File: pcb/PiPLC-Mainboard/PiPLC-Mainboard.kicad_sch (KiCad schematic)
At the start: 145 parts, among them J1 WJ2EDGRC-5.08-4P, J10 WJ2EDGRC-5.08-4P, J11 WJ2EDGRC-5.08-4P, J12 WJ2EDGRC-5.08-4P, J13 Modbus, J17 Conn_02x12_Odd_Even, J3 WJ2EDGRC-5.08-4P, J4 WJ2EDGRC-5.08-4P, J5 WJ2EDGRC-5.08-4P, J6 WJ2EDGRC-5.08-4P, J7 WJ2EDGRC-5.08-4P, J8 WJ2EDGRC-5.08-4P, J9 WJ2EDGRC-5.08-4P, J99 Rpi GPIO, K1 G5RL-1A-E-TV8 DC24, K2 G5RL-1A-E-TV8 DC24, K3 G5RL-1A-E-TV8 DC24, K4 G5RL-1A-E-TV8 DC24, K5 G5RL-1A-E-TV8 DC24, K6 G5RL-1A-E-TV8 DC24, K7 G5RL-1A-E-TV8 DC24, K8 G5RL-1A-E-TV8 DC24, Q1 AO3400A, Q2 AO3400A, Q3 AO3400A, Q4 AO3400A, Q5 AO3400A, Q6 AO3400A, Q7 AO3400A, Q8 AO3400A, U1 TPS54331D, U10 EL817C, U11 EL817C, U12 ISO3082DWR, U2 NCN5121, U3 ISO1540, U4 EL817C, U5 EL817C, U6 EL817C, U7 EL817C, U8 EL817C, U9 EL817C, Y2 16MHz

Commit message: [Main] Start positioning parts
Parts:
- renumbered J3 to J1, J8 to J10, J6 to J11, J7 to J12, J13 to J2, J9 to J3, J10 to J4, J11 to J5, J12 to J6, J1 to J7, J4 to J8, J5 to J9
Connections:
- net +3V3: now also J17.7 (Pin_7); no longer J17.8 (Pin_8)
- net GND: now also J17.4 (Pin_4), J17.6 (Pin_6); no longer J17.3 (Pin_3), J17.5 (Pin_5)
- net KNX +: now also J17.8 (Pin_8); no longer J17.7 (Pin_7)
- net LED_I1: now also J17.9 (Pin_9); no longer J17.10 (Pin_10)
- net LED_I2: now also J17.11 (Pin_11); no longer J17.12 (Pin_12)
- net LED_I3: now also J17.13 (Pin_13); no longer J17.14 (Pin_14)
- net LED_I4: now also J17.15 (Pin_15); no longer J17.16 (Pin_16)
- net LED_I5: now also J17.17 (Pin_17); no longer J17.18 (Pin_18)
- net LED_I6: now also J17.19 (Pin_19); no longer J17.20 (Pin_20)
- net LED_I7: now also J17.21 (Pin_21); no longer J17.22 (Pin_22)
- net LED_I8: now also J17.23 (Pin_23); no longer J17.24 (Pin_24)
- net LED_Q1: now also J17.24 (Pin_24); no longer J17.23 (Pin_23)
- net LED_Q2: now also J17.22 (Pin_22); no longer J17.21 (Pin_21)
- net LED_Q3: now also J17.20 (Pin_20); no longer J17.19 (Pin_19)
- net LED_Q4: now also J17.18 (Pin_18); no longer J17.17 (Pin_17)
- net LED_Q5: now also J17.16 (Pin_16); no longer J17.15 (Pin_15)
- net LED_Q6: now also J17.14 (Pin_14); no longer J17.13 (Pin_13)
- net LED_Q7: now also J17.12 (Pin_12); no longer J17.11 (Pin_11)
- net LED_Q8: now also J17.10 (Pin_10); no longer J17.9 (Pin_9)
- net at R8.1: now also J12.4 (Pin_4); no longer J12.1 (Pin_1)
- net at R9.1: now also J12.3 (Pin_3); no longer J12.2 (Pin_2)
- net at R49.2: now also J17.3 (Pin_3); no longer J17.4 (Pin_4)
- net at R45.2: now also J17.5 (Pin_5); no longer J17.6 (Pin_6)
- net at R10.1: now also J12.2 (Pin_2); no longer J12.3 (Pin_3)
- net at R11.1: now also J12.1 (Pin_1); no longer J12.4 (Pin_4)
- net at R13.1: now also J11.3 (Pin_3); no longer J11.2 (Pin_2)
- net at R15.1: now also J11.1 (Pin_1); no longer J11.4 (Pin_4)
- net at R12.1: now also J11.4 (Pin_4); no longer J11.1 (Pin_1)
- net at R14.1: now also J11.2 (Pin_2); no longer J11.3 (Pin_3)
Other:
- moved on the sheet: J11, J12
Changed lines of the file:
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@@
   (symbol (lib_id "Connector_Generic:Conn_01x04") (at 27.94 157.48 0) (mirror y) (unit 1)
     (in_bom yes) (on_board yes) (dnp no)
-    (property "Reference" "J4" (at 27.94 149.86 0)
+    (property "Reference" "J8" (at 27.94 149.86 0)
       (effects (font (size 1.27 1.27)))
     )
@@
       (project "PiPLC-Mainboard"
         (path "/93ebf745-625a-4d9e-8f47-45e91f30ef94"
-          (reference "J4") (unit 1)
+          (reference "J8") (unit 1)
         )
       )
@@
   (symbol (lib_id "Connector_Generic:Conn_01x04") (at 381 353.06 270) (unit 1)
     (in_bom yes) (on_board yes) (dnp no)
-    (property "Reference" "J10" (at 379.73 364.49 90)
+    (property "Reference" "J4" (at 379.73 364.49 90)
       (effects (font (size 1.27 1.27)))
     )
@@
       (project "PiPLC-Mainboard"
         (path "/93ebf745-625a-4d9e-8f47-45e91f30ef94"
-          (reference "J10") (unit 1)
+          (reference "J4") (unit 1)
         )
       )
@@
   (symbol (lib_id "Connector_Generic:Conn_01x04") (at 259.08 353.06 270) (unit 1)
     (in_bom yes) (on_board yes) (dnp no)
-    (property "Reference" "J11" (at 257.81 364.49 90)
+    (property "Reference" "J5" (at 257.81 364.49 90)
       (effects (font (size 1.27 1.27)))
     )
@@
       (project "PiPLC-Mainboard"
         (path "/93ebf745-625a-4d9e-8f47-45e91f30ef94"
-          (reference "J11") (unit 1)
+          (reference "J5") (unit 1)
         )
       )
@@
   (symbol (lib_id "Connector_Generic:Conn_01x04") (at 27.94 189.23 0) (mirror y) (unit 1)
     (in_bom yes) (on_board yes) (dnp no)
-    (property "Reference" "J5" (at 27.94 181.61 0)
+    (property "Reference" "J9" (at 27.94 181.61 0)
       (effects (font (size 1.27 1.27)))
     )
@@
       (project "PiPLC-Mainboard"
         (path "/93ebf745-625a-4d9e-8f47-45e91f30ef94"
-          (reference "J5") (unit 1)
+          (reference "J9") (unit 1)
         )
       )
@@
   (symbol (lib_id "Connector_Generic:Conn_01x04") (at 502.92 353.06 270) (unit 1)
     (in_bom yes) (on_board yes) (dnp no)
-    (property "Reference" "J9" (at 501.65 364.49 90)
+    (property "Reference" "J3" (at 501.65 364.49 90)
       (effects (font (size 1.27 1.27)))
     )
@@
       (project "PiPLC-Mainboard"
         (path "/93ebf745-625a-4d9e-8f47-45e91f30ef94"
-          (reference "J9") (unit 1)
+          (reference "J3") (unit 1)
         )
       )
@@
   (symbol (lib_id "Connector_Generic:Conn_01x04") (at 410.21 160.02 0) (unit 1)
     (in_bom yes) (on_board yes) (dnp no)
-    (property "Reference" "J1" (at 410.21 152.4 0)
+    (property "Reference" "J7" (at 410.21 152.4 0)
       (effects (font (size 1.27 1.27)))
     )
@@
       (project "PiPLC-Mainboard"
         (path "/93ebf745-625a-4d9e-8f47-45e91f30ef94"
-          (reference "J1") (unit 1)
+          (reference "J7") (unit 1)
         )
       )
@@
     )
   )
-  (symbol (lib_id "Connector_Generic:Conn_02x12_Odd_Even") (at 193.04 241.3 90) (unit 1)
-    (in_bom yes) (on_board yes) (dnp no) (fields_autoplaced)
-    (property "Reference" "J17" (at 177.8 238.76 90)
+  (symbol (lib_id "Connector_Generic:Conn_02x12_Odd_Even") (at 193.04 238.76 90) (mirror x) (unit 1)
+    (in_bom yes) (on_board yes) (dnp no)
+    (property "Reference" "J17" (at 177.8 241.3 90)
       (effects (font (size 1.27 1.27)) (justify left))
     )
-    (property "Value" "Conn_02x12_Odd_Even" (at 177.8 241.3 90)
+    (property "Value" "Conn_02x12_Odd_Even" (at 177.8 238.76 90)
       (effects (font (size 1.27 1.27)) (justify left))
     )
-    (property "Footprint" "Connector_PinSocket_2.54mm:PinSocket_2x12_P2.54mm_Vertical" (at 193.04 241.3 0)
+    (property "Footprint" "Connector_PinSocket_2.54mm:PinSocket_2x12_P2.54mm_Vertical" (at 193.04 238.76 0)
       (effects (font (size 1.27 1.27)) hide)
     )
-    (property "Datasheet" "~" (at 193.04 241.3 0)
+    (property "Datasheet" "~" (at 193.04 238.76 0)
       (effects (font (size 1.27 1.27)) hide)
     )
@@
     )
   )
-  (symbol (lib_id "Connector_Generic:Conn_01x04") (at 27.94 30.48 0) (mirror y) (unit 1)
+  (symbol (lib_id "Connector_Generic:Conn_01x04") (at 27.94 33.02 180) (unit 1)
     (in_bom yes) (on_board yes) (dnp no)
-    (property "Reference" "J7" (at 27.94 22.86 0)
+    (property "Reference" "J12" (at 27.94 22.86 0)
       (effects (font (size 1.27 1.27)))
     )
@@
       (effects (font (size 1.27 1.27)))
     )
-    (property "Footprint" "Connector_Phoenix_MSTB:PhoenixContact_MSTBA_2,5_4-G-5,08_1x04_P5.08mm_Horizontal" (at 27.94 30.48 0)
+    (property "Footprint" "Connector_Phoenix_MSTB:PhoenixContact_MSTBA_2,5_4-G-5,08_1x04_P5.08mm_Horizontal" (at 27.94 33.02 0)
       (effects (font (size 1.27 1.27)) hide)
     )
-    (property "Datasheet" "https://datasheet.lcsc.com/lcsc/1912251635_Ningbo-Kangnex-Elec-WJ2EDGRC-5-08-4P_C8446.pdf" (at 27.94 30.48 0)
+    (property "Datasheet" "https://datasheet.lcsc.com/lcsc/1912251635_Ningbo-Kangnex-Elec-WJ2EDGRC-5-08-4P_C8446.pdf" (at 27.94 33.02 0)
       (effects (font (size 1.27 1.27)) hide)
     )
-    (property "LCSC" "C8446" (at 27.94 30.48 0)
+    (property "LCSC" "C8446" (at 27.94 33.02 0)
       (effects (font (size 1.27 1.27)) hide)
     )
@@
       (project "PiPLC-Mainboard"
         (path "/93ebf745-625a-4d9e-8f47-45e91f30ef94"
-          (reference "J7") (unit 1)
+          (reference "J12") (unit 1)
         )
       )
@@
   (symbol (lib_id "Connector_Generic:Conn_01x04") (at 236.22 31.75 0) (mirror y) (unit 1)
     (in_bom yes) (on_board yes) (dnp no)
-    (property "Reference" "J8" (at 231.14 24.13 0)
+    (property "Reference" "J10" (at 231.14 24.13 0)
       (effects (font (size 1.27 1.27)))
     )
@@
       (project "PiPLC-Mainboard"
         (path "/93ebf745-625a-4d9e-8f47-45e91f30ef94"
-          (reference "J8") (unit 1)
+          (reference "J10") (unit 1)
         )
       )
@@
   (symbol (lib_id "Connector_Generic:Conn_01x04") (at 27.94 220.98 0) (mirror y) (unit 1)
     (in_bom yes) (on_board yes) (dnp no)
-    (property "Reference" "J3" (at 27.94 213.36 0)
+    (property "Reference" "J1" (at 27.94 213.36 0)
       (effects (font (size 1.27 1.27)))
     )
@@
       (project "PiPLC-Mainboard"
         (path "/93ebf745-625a-4d9e-8f47-45e91f30ef94"
-          (reference "J3") (unit 1)
+          (reference "J1") (unit 1)
         )
       )
@@
   (symbol (lib_id "Connector_Generic:Conn_01x04") (at 137.16 353.06 270) (unit 1)
     (in_bom yes) (on_board yes) (dnp no)
-    (property "Reference" "J12" (at 135.89 364.49 90)
+    (property "Reference" "J6" (at 135.89 364.49 90)
       (effects (font (size 1.27 1.27)))
     )
@@
       (project "PiPLC-Mainboard"
         (path "/93ebf745-625a-4d9e-8f47-45e91f30ef94"
-          (reference "J12") (unit 1)
+          (reference "J6") (unit 1)
         )
       )
@@
   (symbol (lib_id "Connector_Generic:Conn_01x04") (at 411.48 195.58 0) (unit 1)
     (in_bom yes) (on_board yes) (dnp no)
-    (property "Reference" "J13" (at 411.48 187.96 0)
+    (property "Reference" "J2" (at 411.48 187.96 0)
       (effects (font (size 1.27 1.27)))
     )
@@
       (project "PiPLC-Mainboard"
         (path "/93ebf745-625a-4d9e-8f47-45e91f30ef94"
-          (reference "J13") (unit 1)
+          (reference "J2") (unit 1)
         )
       )
@@
     )
   )
-  (symbol (lib_id "Connector_Generic:Conn_01x04") (at 123.19 30.48 0) (mirror y) (unit 1)
+  (symbol (lib_id "Connector_Generic:Conn_01x04") (at 123.19 33.02 180) (unit 1)
     (in_bom yes) (on_board yes) (dnp no)
-    (property "Reference" "J6" (at 121.92 22.86 0)
+    (property "Reference" "J11" (at 121.92 22.86 0)
       (effects (font (size 1.27 1.27)))
     )
-    (property "Value" "WJ2EDGRC-5.08-4P" (at 120.65 25.4 0)
+    (property "Value" "WJ2EDGRC-5.08-4P" (at 121.92 25.4 0)
       (effects (font (size 1.27 1.27)))
     )
-    (property "Footprint" "Connector_Phoenix_MSTB:PhoenixContact_MSTBA_2,5_4-G-5,08_1x04_P5.08mm_Horizontal" (at 123.19 30.48 0)
+    (property "Footprint" "Connector_Phoenix_MSTB:PhoenixContact_MSTBA_2,5_4-G-5,08_1x04_P5.08mm_Horizontal" (at 123.19 33.02 0)
       (effects (font (size 1.27 1.27)) hide)
     )
-    (property "Datasheet" "https://datasheet.lcsc.com/lcsc/1912251635_Ningbo-Kangnex-Elec-WJ2EDGRC-5-08-4P_C8446.pdf" (at 123.19 30.48 0)
+    (property "Datasheet" "https://datasheet.lcsc.com/lcsc/1912251635_Ningbo-Kangnex-Elec-WJ2EDGRC-5-08-4P_C8446.pdf" (at 123.19 33.02 0)
       (effects (font (size 1.27 1.27)) hide)
     )
-    (property "LCSC" "C8446" (at 123.19 30.48 0)
+    (property "LCSC" "C8446" (at 123.19 33.02 0)
       (effects (font (size 1.27 1.27)) hide)
     )
@@
       (project "PiPLC-Mainboard"
         (path "/93ebf745-625a-4d9e-8f47-45e91f30ef94"
-          (reference "J6") (unit 1)
+          (reference "J11") (unit 1)
         )
       )

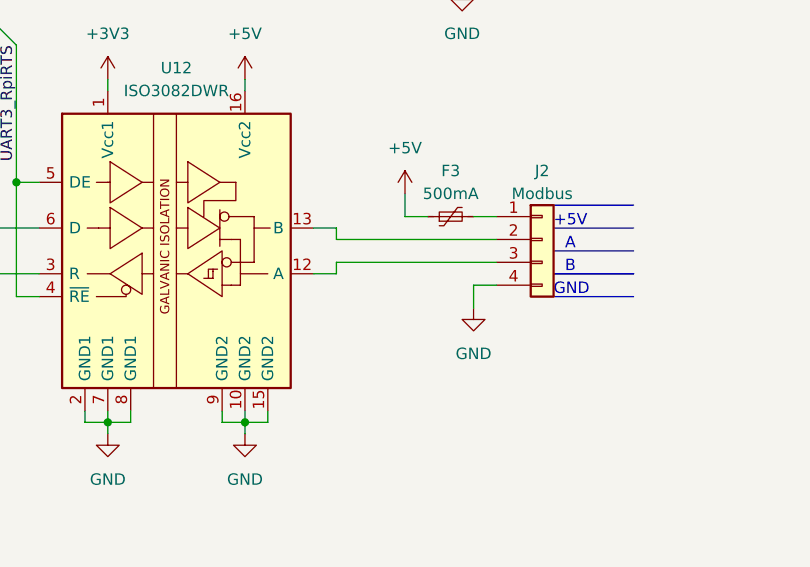
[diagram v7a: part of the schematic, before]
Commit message: Add termination resistor to Modbus terminal
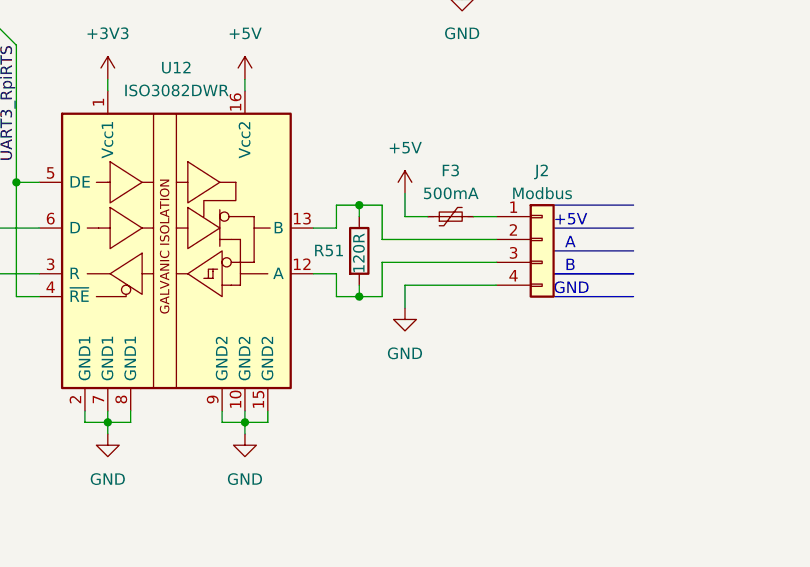
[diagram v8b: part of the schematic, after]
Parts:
- added R51: 120R, Resistor_SMD:R_0603_1608Metric, symbol Device:R
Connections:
- net at J2.2 (Pin_2), U12.13 (B): now also R51.1
- net at J2.3 (Pin_3), U12.12 (A): now also R51.2
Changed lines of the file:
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@@
   (junction (at 398.78 297.18) (diameter 0) (color 0 0 0 0)
   )
+  (junction (at 391.16 201.93) (diameter 0) (color 0 0 0 0)
+  )
   (junction (at 363.22 215.9) (diameter 0) (color 0 0 0 0)
   )
@@
   (junction (at 228.6 107.95) (diameter 0) (color 0 0 0 0)
   )
+  (junction (at 391.16 191.77) (diameter 0) (color 0 0 0 0)
+  )
   (junction (at 374.65 138.43) (diameter 0) (color 0 0 0 0)
   )
@@
     (stroke (width 0) (type default))
   )
+  (wire (pts (xy 391.16 191.77) (xy 393.7 191.77))
+    (stroke (width 0) (type default))
+  )
   (wire (pts (xy 505.46 347.98) (xy 505.46 345.44))
     (stroke (width 0) (type default))
@@
     (stroke (width 0) (type default))
   )
+  (wire (pts (xy 393.7 191.77) (xy 393.7 195.58))
+    (stroke (width 0) (type default))
+  )
   (wire (pts (xy 54.61 218.44) (xy 64.77 218.44))
     (stroke (width 0) (type solid))
@@
     (stroke (width 0) (type default))
   )
+  (wire (pts (xy 391.16 200.66) (xy 391.16 201.93))
+    (stroke (width 0) (type default))
+  )
   (wire (pts (xy 148.59 71.12) (xy 151.13 71.12))
     (stroke (width 0) (type default))
@@
     (stroke (width 0) (type default))
   )
+  (wire (pts (xy 393.7 198.12) (xy 406.4 198.12))
+    (stroke (width 0) (type default))
+  )
   (wire (pts (xy 396.24 110.49) (xy 391.16 110.49))
     (stroke (width 0) (type default))
@@
     (stroke (width 0) (type default))
   )
+  (wire (pts (xy 393.7 195.58) (xy 406.4 195.58))
+    (stroke (width 0) (type default))
+  )
   (polyline (pts (xy 499.11 360.68) (xy 499.11 354.33))
     (stroke (width 0) (type solid))
@@
     (stroke (width 0) (type default))
   )
+  (wire (pts (xy 391.16 191.77) (xy 391.16 193.04))
+    (stroke (width 0) (type default))
+  )
   (wire (pts (xy 53.34 173.99) (xy 274.32 173.99))
     (stroke (width 0) (type default))
@@
     (stroke (width 0) (type solid))
   )
+  (wire (pts (xy 388.62 199.39) (xy 388.62 201.93))
+    (stroke (width 0) (type default))
+  )
   (wire (pts (xy 45.72 218.44) (xy 54.61 218.44))
     (stroke (width 0) (type solid))
@@
     (stroke (width 0) (type solid))
   )
+  (wire (pts (xy 386.08 199.39) (xy 388.62 199.39))
+    (stroke (width 0) (type default))
+  )
   (wire (pts (xy 311.15 285.75) (xy 311.15 312.42))
     (stroke (width 0) (type default))
@@
     (stroke (width 0) (type default))
   )
+  (wire (pts (xy 391.16 201.93) (xy 393.7 201.93))
+    (stroke (width 0) (type default))
+  )
   (wire (pts (xy 71.12 27.94) (xy 76.2 27.94))
     (stroke (width 0) (type default))
@@
     (stroke (width 0) (type default))
   )
+  (wire (pts (xy 388.62 201.93) (xy 391.16 201.93))
+    (stroke (width 0) (type default))
+  )
   (wire (pts (xy 398.78 313.69) (xy 398.78 314.96))
     (stroke (width 0) (type default))
@@
     (stroke (width 0) (type solid))
   )
+  (wire (pts (xy 386.08 194.31) (xy 388.62 194.31))
+    (stroke (width 0) (type default))
+  )
   (wire (pts (xy 377.19 66.04) (xy 377.19 58.42))
     (stroke (width 0) (type default))
@@
     (stroke (width 0) (type default))
   )
-  (wire (pts (xy 388.62 198.12) (xy 388.62 199.39))
-    (stroke (width 0) (type default))
-  )
   (wire (pts (xy 72.39 33.02) (xy 72.39 34.29))
     (stroke (width 0) (type default))
@@
     (stroke (width 0) (type default))
   )
-  (wire (pts (xy 386.08 194.31) (xy 388.62 194.31))
-    (stroke (width 0) (type default))
-  )
   (wire (pts (xy 351.79 113.03) (xy 351.79 120.65))
     (stroke (width 0) (type default))
@@
     (stroke (width 0) (type solid))
   )
-  (wire (pts (xy 406.4 198.12) (xy 388.62 198.12))
-    (stroke (width 0) (type default))
-  )
   (wire (pts (xy 387.35 71.12) (xy 387.35 68.58))
     (stroke (width 0) (type default))
@@
     (stroke (width 0) (type default))
   )
-  (wire (pts (xy 403.86 200.66) (xy 406.4 200.66))
+  (wire (pts (xy 396.24 200.66) (xy 406.4 200.66))
     (stroke (width 0) (type default))
   )
@@
     (stroke (width 0) (type default))
   )
-  (wire (pts (xy 403.86 203.2) (xy 403.86 200.66))
+  (wire (pts (xy 396.24 203.2) (xy 396.24 200.66))
     (stroke (width 0) (type default))
   )
@@
     (stroke (width 0) (type default))
   )
+  (wire (pts (xy 393.7 201.93) (xy 393.7 198.12))
+    (stroke (width 0) (type default))
+  )
   (wire (pts (xy 494.03 312.42) (xy 500.38 312.42))
     (stroke (width 0) (type default))
@@
     (stroke (width 0) (type default))
   )
-  (wire (pts (xy 388.62 195.58) (xy 388.62 194.31))
-    (stroke (width 0) (type default))
-  )
   (wire (pts (xy 422.91 90.17) (xy 430.53 90.17))
     (stroke (width 0) (type default))
@@
     (stroke (width 0) (type default))
   )
-  (wire (pts (xy 388.62 199.39) (xy 386.08 199.39))
-    (stroke (width 0) (type default))
-  )
   (polyline (pts (xy 20.32 34.29) (xy 26.67 34.29))
     (stroke (width 0) (type solid))
@@
     (stroke (width 0) (type default))
   )
-  (wire (pts (xy 388.62 195.58) (xy 406.4 195.58))
-    (stroke (width 0) (type default))
-  )
   (wire (pts (xy 104.14 313.69) (xy 104.14 345.44))
     (stroke (width 0) (type default))
@@
     (stroke (width 0) (type default))
   )
+  (wire (pts (xy 388.62 194.31) (xy 388.62 191.77))
+    (stroke (width 0) (type default))
+  )
   (wire (pts (xy 513.08 314.96) (xy 513.08 309.88))
     (stroke (width 0) (type default))
@@
     (stroke (width 0) (type default))
   )
+  (wire (pts (xy 388.62 191.77) (xy 391.16 191.77))
+    (stroke (width 0) (type default))
+  )
   (wire (pts (xy 132.08 347.98) (xy 132.08 345.44))
     (stroke (width 0) (type default))
@@
     )
   )
+  (symbol (lib_id "Device:R") (at 391.16 196.85 0) (unit 1)
+    (in_bom yes) (on_board yes) (dnp no)
+    (property "Reference" "R51" (at 386.08 196.85 0)
+      (effects (font (size 1.27 1.27)) (justify left))
+    )
+    (property "Value" "120R" (at 391.16 199.39 90)
+      (effects (font (size 1.27 1.27)) (justify left))
+    )
+    (property "Footprint" "Resistor_SMD:R_0603_1608Metric" (at 389.382 196.85 90)
+      (effects (font (size 1.27 1.27)) hide)
+    )
+    (property "Datasheet" "~" (at 391.16 196.85 0)
+      (effects (font (size 1.27 1.27)) hide)
+    )
+    (property "LCSC" "C22787" (at 391.16 196.85 0)
+      (effects (font (size 1.27 1.27)) hide)
+    )
+    (pin "1")
+    (pin "2")
+    (instances
+      (project "PiPLC-Mainboard"
+        (path "/93ebf745-625a-4d9e-8f47-45e91f30ef94"
+          (reference "R51") (unit 1)
+        )
+      )
+    )
+  )
   (symbol (lib_id "power:+5V") (at 119.38 203.2 0) (unit 1)
     (in_bom yes) (on_board yes) (dnp no)
@@
     )
   )
-  (symbol (lib_id "power:GND") (at 403.86 203.2 0) (unit 1)
+  (symbol (lib_id "power:GND") (at 396.24 203.2 0) (unit 1)
     (in_bom yes) (on_board yes) (dnp no) (fields_autoplaced)
-    (property "Reference" "#PWR052" (at 403.86 209.55 0)
+    (property "Reference" "#PWR052" (at 396.24 209.55 0)
       (effects (font (size 1.27 1.27)) hide)
     )
-    (property "Value" "GND" (at 403.86 208.28 0)
+    (property "Value" "GND" (at 396.24 208.28 0)
       (effects (font (size 1.27 1.27)))
     )
-    (property "Footprint" "" (at 403.86 203.2 0)
+    (property "Footprint" "" (at 396.24 203.2 0)
       (effects (font (size 1.27 1.27)) hide)
     )
-    (property "Datasheet" "" (at 403.86 203.2 0)
+    (property "Datasheet" "" (at 396.24 203.2 0)
       (effects (font (size 1.27 1.27)) hide)
     )
